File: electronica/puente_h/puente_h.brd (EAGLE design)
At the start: 100 x 80 mm, 40 parts, among them IC1 7805, IC2 7812, IC3 74HC04N, IC4 74HC08N, IC5 ADUM1400, Q1 IRF2804, Q2 IRF2804, Q5 IRF2804, Q6 IRF2804, U3 IR2110

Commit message: pads mas largos
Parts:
- removed JP2: (no value), pinhead:1X06
- removed U3: IR2110, components:IR2110
- added JP1: (no value), pinhead:1X06
- added U1: IR2110LP, components:IR2110-LP
- U$1: value IR2110 -> IR2110LP; device components:IR2110 -> components:IR2110-LP
- moved R18 137.3 mm to (66.3, 37.0), turned to 90 degrees
- moved C8 134.8 mm to (67.3, 106.7)
- moved Q5 121.9 mm to (57.1, 38.5), turned to 90 degrees
- moved MOTOR 121.4 mm to (38.2, 11.0), turned to 180 degrees
- moved R20 121.3 mm to (70.9, 20.6), turned to 270 degrees
- moved IC5 118.4 mm to (24.4, 106.2), turned to 180 degrees
- moved C3 118.1 mm to (53.1, 110.7), turned to 180 degrees
- moved R17 118.0 mm to (65.3, 52.5), turned to 180 degrees
- moved D9 105.1 mm to (66.5, 21.0), turned to 270 degrees
- moved D7 105.1 mm to (33.1, 57.7), turned to 180 degrees
- moved IC3 104.6 mm to (13.0, 86.2)
- moved IC2 102.4 mm to (50.3, 102.4), turned to 180 degrees
- moved R19 100.2 mm to (70.6, 36.7), turned to 270 degrees
- moved C1 99.1 mm to (49.1, 93.7)
- moved IN 92.0 mm to (61.0, 118.1), turned to 180 degrees
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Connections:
- removed net GND1@2: C7.2, IC5.2, IC5.8, JP2.2
- removed net N$13: IC5.4, JP2.4
- removed net N$14: IC5.5, JP2.5
- removed net N$8: IC5.3, JP2.3
- new net N$20: IC5.6, JP1.1
- new net N$21: IC5.4, JP1.3
- new net N$22: IC5.3, JP1.4
- new net N$24: C7.1, IC5.1, JP1.6
- net +12V: now also U1.3; no longer U3.3
- net +5V: now also U1.9; no longer U3.9
- net GND: now also U1.13, U1.2; no longer U3.13, U3.2
- net N$1: now also U1.6; no longer U$1.6
- net N$11: now also U1.10; no longer U$1.10
- net N$12: now also U1.12; no longer U$1.12
- net N$15: now also IC5.5, JP1.2; no longer IC5.6, JP2.6
- net N$19: now also U$1.12; no longer U3.12
- net N$2: now also U1.7; no longer U$1.7
- net N$3: now also U1.5; no longer U$1.5
- net N$30: now also U$1.6; no longer U3.6
- net N$31: now also U$1.5; no longer U3.5
- net N$32: now also U$1.7; no longer U3.7
- net N$35: now also U$1.1; no longer U3.1
- net N$5: now also C7.2, IC5.2, IC5.8, JP1.5; no longer C7.1, IC5.1, JP2.1
- net N$6: now also U1.1; no longer U$1.1
- net N$9: now also U$1.10; no longer U3.10
- net SD: now also U1.11; no longer U3.11
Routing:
- net GND: track 0.00 -> 246.0 mm
- net +5V: track 0.00 -> 112.4 mm
- net +12V: track 0.00 -> 80.4 mm
- net N$35: track 0.00 -> 76.8 mm
- net N$3: track 0.00 -> 70.1 mm
- net N$31: track 0.00 -> 65.8 mm
- net N$6: track 0.00 -> 49.8 mm
- net A: track 0.00 -> 42.7 mm, vias 0 -> 1
- net B: track 0.00 -> 41.2 mm
- net N$30: track 0.00 -> 40.7 mm
- net EN: track 0.00 -> 38.3 mm
- net N$4: track 0.00 -> 31.2 mm
- net N$12: track 0.00 -> 30.8 mm
- net N$7: track 0.00 -> 30.1 mm
- net N$5: track 0.00 -> 27.8 mm
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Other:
- board size 100 x 80 mm -> 80.2 x 123.2 mm

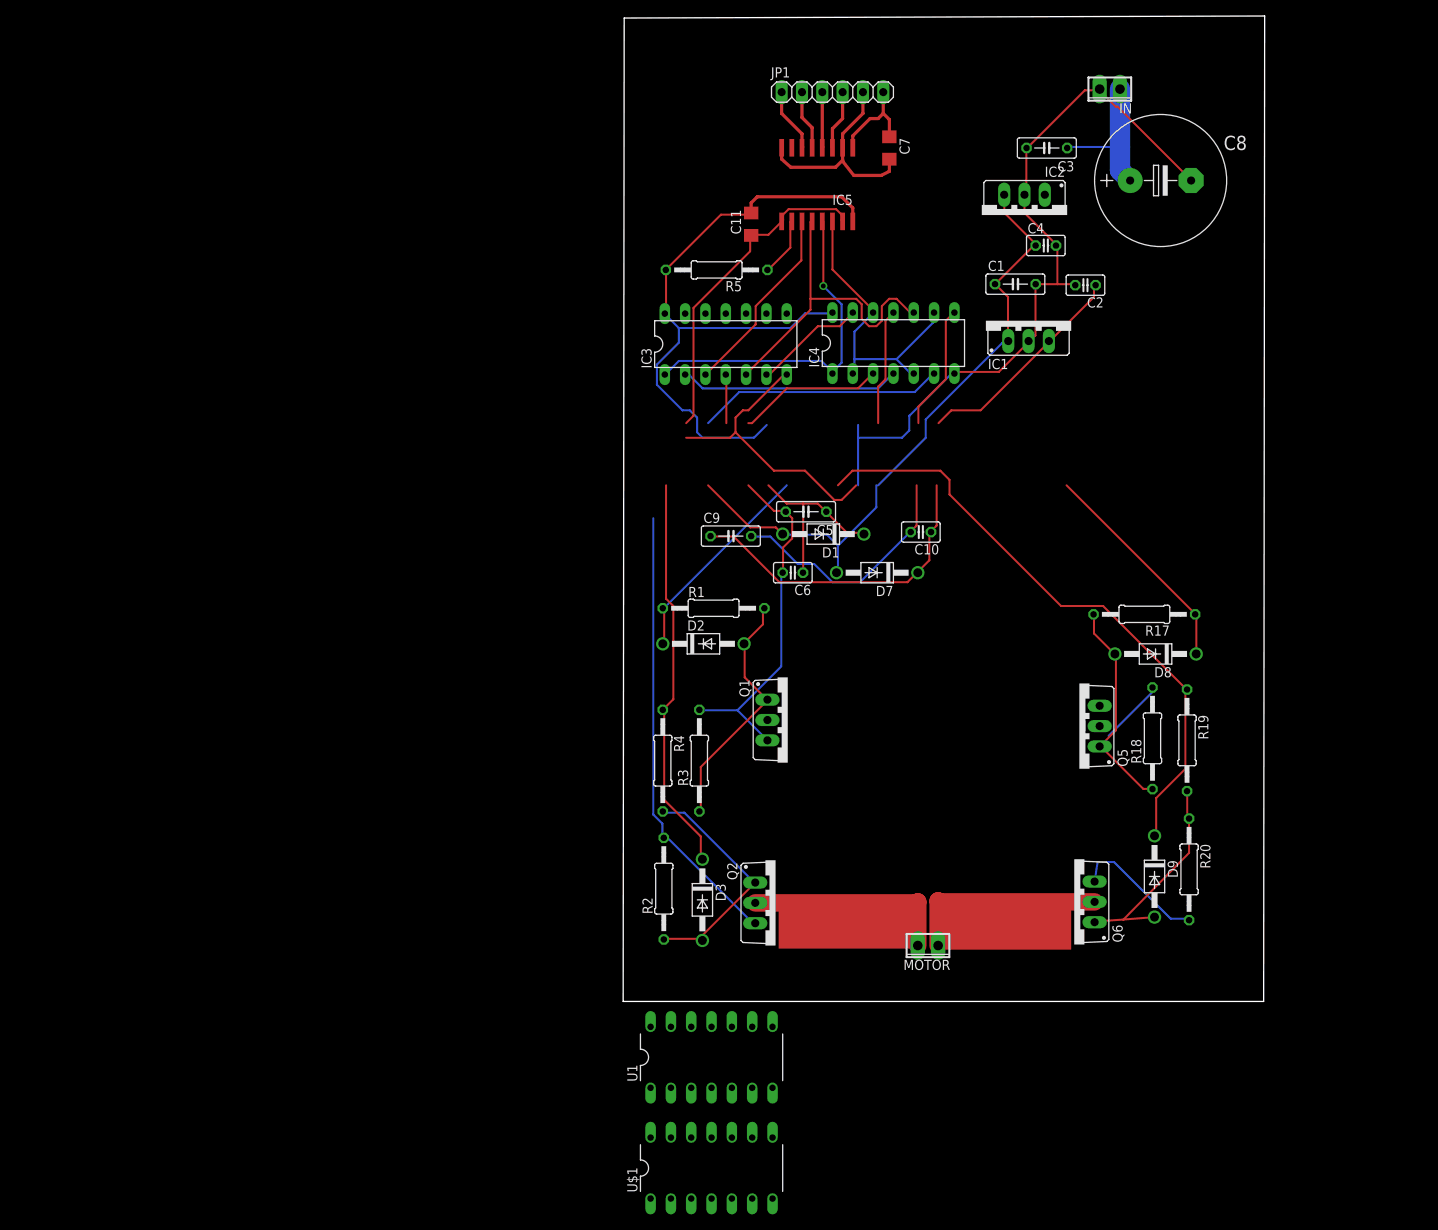
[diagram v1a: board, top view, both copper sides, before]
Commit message: packages con pad mas largos, nuevo pcb
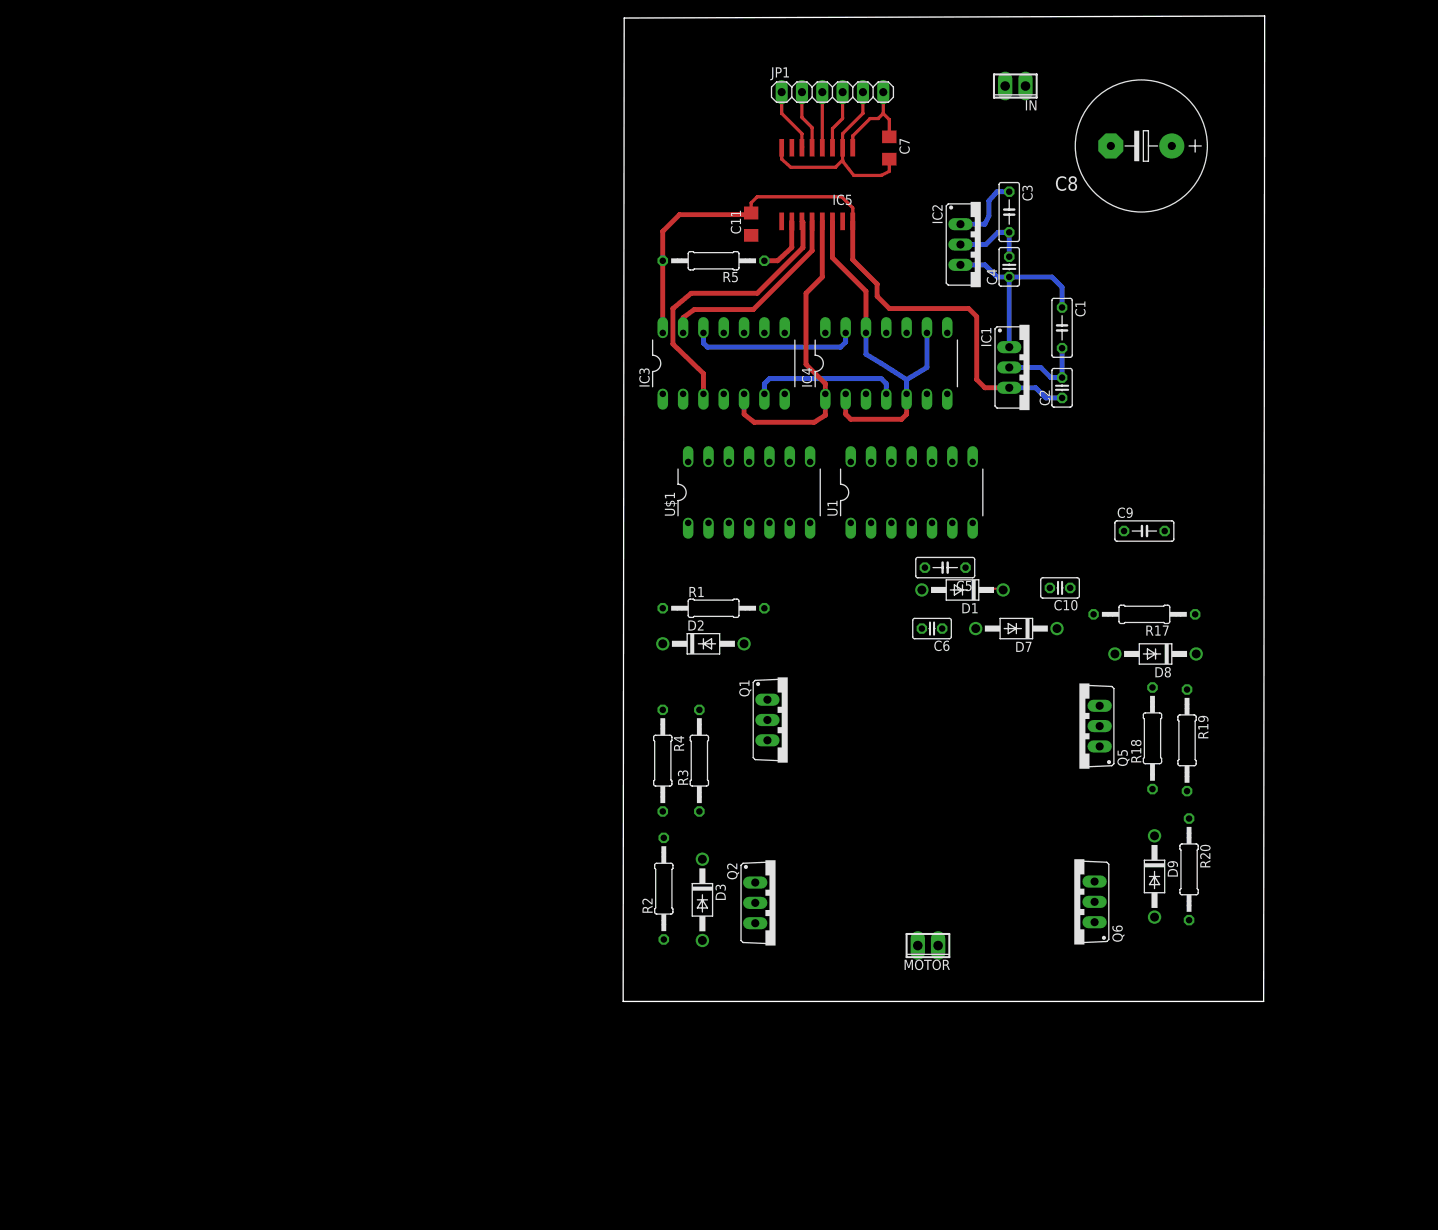
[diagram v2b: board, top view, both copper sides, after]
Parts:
- IC3: value 74HC04N -> 7404LP; device 74xx-eu:DIL14 -> components:IR2110-LP
- IC4: value 74HC08N -> 7408LP; device 74xx-eu:DIL14 -> components:IR2110-LP
- moved U$1 84.6 mm to (14.6, 67.7)
- moved U1 74.9 mm to (34.9, 67.7)
- moved C9 51.7 mm to (65.3, 62.9)
- moved C5 18.7 mm to (40.4, 58.3)
- moved C10 18.7 mm to (54.7, 55.8)
- moved C6 18.7 mm to (38.7, 50.7)
- moved D1 18.7 mm to (43.8, 55.5)
- moved D7 18.7 mm to (50.5, 50.7)
- moved C2 13.2 mm to (55.0, 80.8), turned to 90 degrees
- moved IN 11.8 mm to (49.1, 118.5)
- moved C3 9.28 mm to (48.4, 102.7), turned to 270 degrees
- moved C1 8.00 mm to (55.0, 88.3), turned to 270 degrees
- moved IC2 6.59 mm to (44.8, 98.7), turned to 270 degrees
- moved IC1 5.84 mm to (50.9, 83.3), turned to 270 degrees
- moved C4 5.29 mm to (48.4, 95.9), turned to 90 degrees
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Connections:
- net A: now also IC3.5; no longer IC3.1
- net B: now also IC3.13; no longer IC3.5
- net N$10: now also IC3.6; no longer IC3.2
- net N$17: now also IC3.12; no longer IC3.6
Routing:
- net GND: track 246.0 -> 20.6 mm
- net N$35: track 76.8 -> 0.00 mm
- net N$3: track 70.1 -> 0.00 mm
- net N$31: track 65.8 -> 0.00 mm
- net +12V: track 80.4 -> 25.2 mm
- net N$6: track 49.8 -> 0.00 mm
- net N$30: track 40.7 -> 0.19 mm
- net N$4: track 31.2 -> 0.00 mm
- net N$12: track 30.8 -> 0.00 mm
- net N$7: track 30.1 -> 1.46 mm
- net N$32: track 27.8 -> 0.15 mm
- net +5V: track 112.4 -> 84.9 mm
- net N$33: track 27.3 -> 0.00 mm
- net N$36: track 27.1 -> 0.55 mm
- net N$2: track 26.4 -> 0.49 mm
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
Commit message: mejores posiciones
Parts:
- moved D1 32.6 mm to (11.3, 58.0)
- moved C6 32.0 mm to (6.86, 53.1)
- moved D8 29.2 mm to (38.9, 45.3)
- moved R17 26.6 mm to (38.9, 49.8)
- moved C5 26.0 mm to (14.9, 53.2)
- moved C9 25.7 mm to (41.1, 54.1), turned to 180 degrees
- moved U1 23.5 mm to (11.4, 67.9)
- moved C10 20.8 mm to (34.0, 54.1)
- moved U$1 17.4 mm to (32.0, 67.9)
- moved D7 14.5 mm to (38.5, 58.8)
- moved R19 13.0 mm to (57.7, 38.2)
- moved R20 12.7 mm to (58.2, 19.6), turned to 90 degrees
- moved R18 12.5 mm to (53.8, 38.4)
- moved D9 12.1 mm to (54.5, 19.8)
- moved Q5 11.6 mm to (45.6, 37.7)
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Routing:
- net GND: track 20.6 -> 67.6 mm
- net SD: track 0.00 -> 31.4 mm
- net N$11: track 0.00 -> 24.8 mm
- net +12V: track 25.2 -> 48.1 mm
- net +5V: track 84.9 -> 98.6 mm
- net N$1: track 2.37 -> 0.00 mm
- net N$7: track 1.46 -> 0.23 mm
- net N$36: track 0.55 -> 0.00 mm
- net N$10: track 18.3 -> 18.8 mm

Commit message: ruteo mejorado
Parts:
- moved IN 53.7 mm to (65.9, 67.4), turned to 90 degrees
- moved C8 44.1 mm to (54.4, 68.2), turned to 90 degrees
- moved C10 25.7 mm to (59.7, 55.9)
- moved D8 18.3 mm to (57.1, 45.7)
- moved R17 15.8 mm to (54.6, 50.8)
- moved D1 13.0 mm to (22.9, 52.1), turned to 270 degrees
- moved C9 9.81 mm to (50.8, 55.9), turned to 0 degrees
- moved D7 9.00 mm to (44.5, 52.1), turned to 270 degrees
- moved MOTOR 4.64 mm to (29.1, 9.14)
- moved D2 4.37 mm to (12.7, 47.0)
- moved R19 4.24 mm to (61.0, 35.6)
- moved Q5 4.05 mm to (42.2, 35.6), turned to 270 degrees
- moved C11 3.39 mm to (15.4, 104.5)
- moved Q6 3.30 mm to (42.2, 17.8), turned to 270 degrees
- moved Q1 3.24 mm to (20.3, 35.6)
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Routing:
- net GND: track 67.6 -> 216.1 mm
- net N$31: track 0.00 -> 136.8 mm
- net VIN: track 9.14 -> 141.6 mm
- net N$3: track 0.00 -> 119.9 mm
- net N$35: track 0.00 -> 83.2 mm
- net +12V: track 48.1 -> 120.8 mm
- net N$6: track 0.00 -> 58.1 mm
- net N$32: track 0.00 -> 44.7 mm, vias 0 -> 1
- net N$2: track 0.00 -> 40.8 mm
- net N$30: track 0.00 -> 30.0 mm
- net N$36: track 0.00 -> 27.3 mm
- net N$33: track 0.00 -> 26.9 mm
- net N$1: track 0.00 -> 26.1 mm
- net N$4: track 0.00 -> 22.9 mm
- net N$19: track 0.00 -> 22.8 mm
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
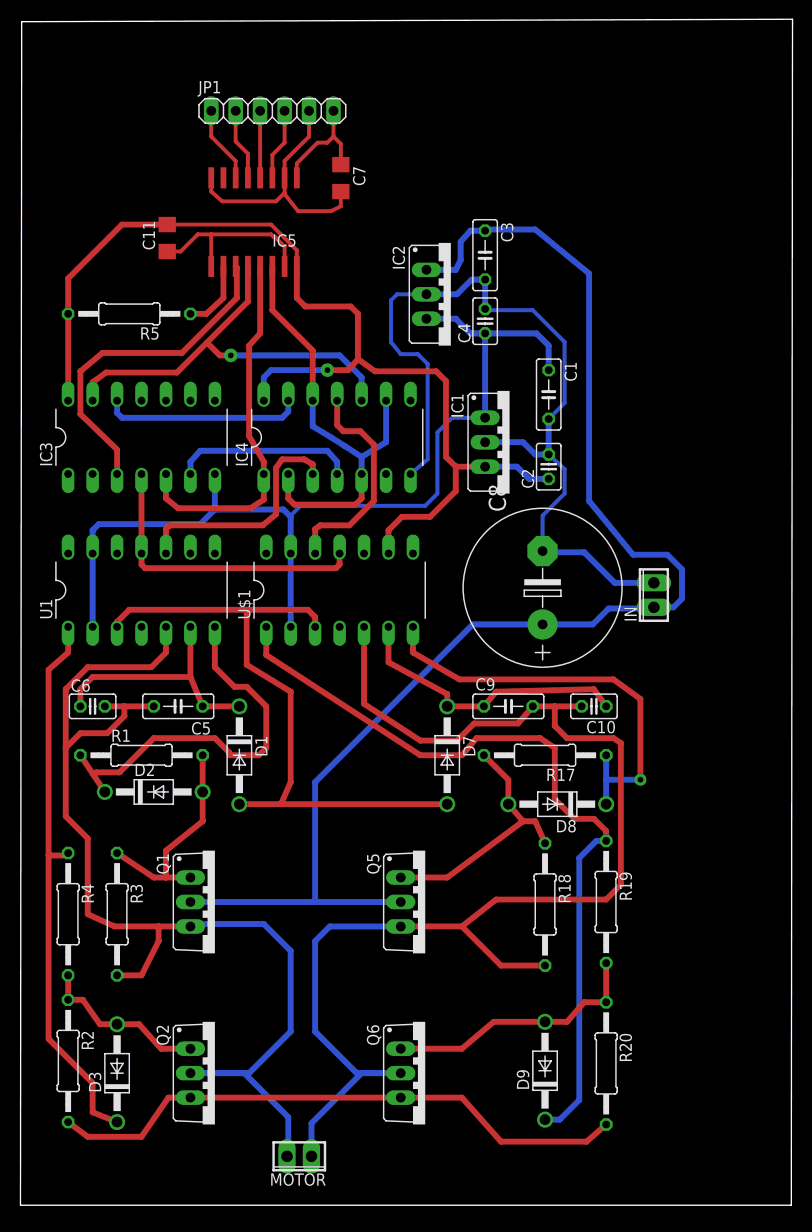
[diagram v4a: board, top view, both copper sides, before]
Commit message: ruteo con poligonos
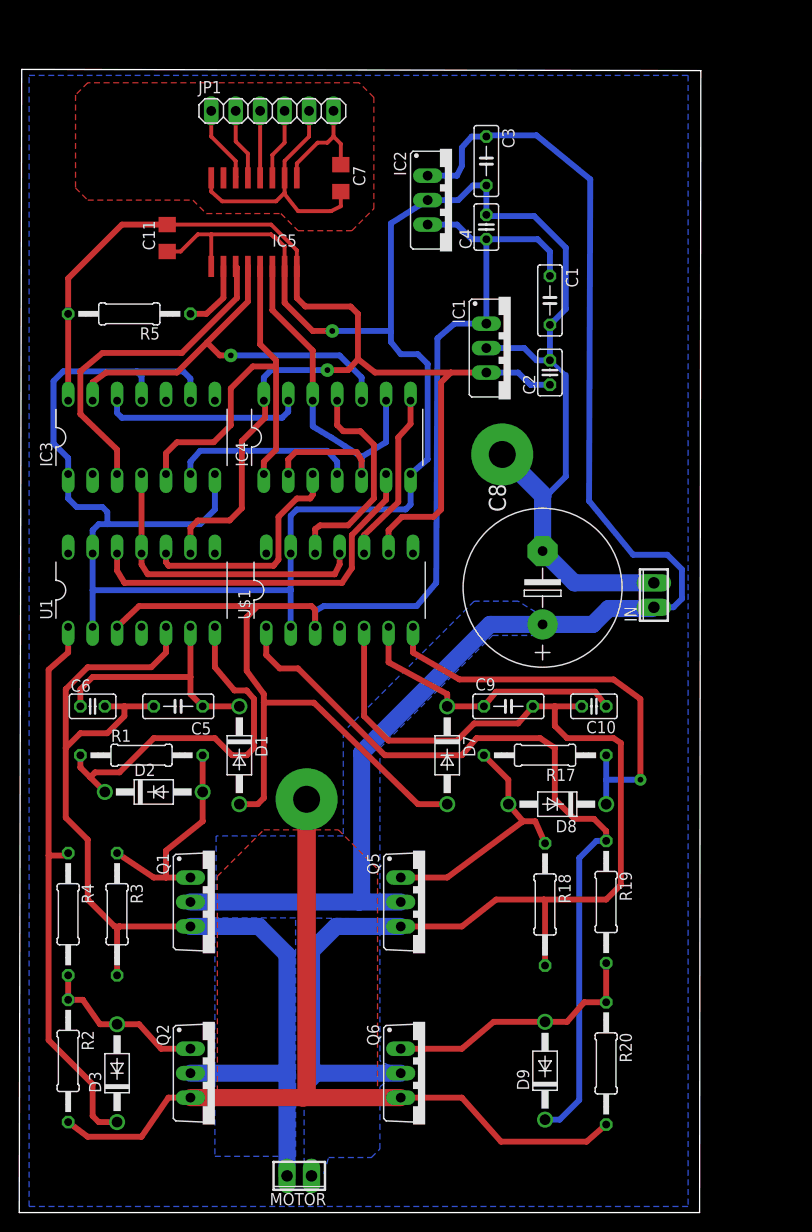
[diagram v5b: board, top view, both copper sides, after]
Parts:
- moved C3 9.78 mm to (48.5, 112.5)
- moved C1 9.78 mm to (55.1, 98.0)
- moved C2 9.78 mm to (55.1, 90.6)
- moved C4 9.78 mm to (48.5, 105.7)
- moved IC1 9.78 mm to (51.1, 93.1)
- moved IC2 9.78 mm to (45.0, 108.5)
- moved MOTOR 2.03 mm to (29.1, 7.11)
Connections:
- net N$3 renamed POWER-M2
- net N$31 renamed POWER-M1
- net N$5 renamed GND-IN
- net GND: now also IC3.1, IC3.11, IC3.9
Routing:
- net GND: track 216.1 -> 355.8 mm, vias 0 -> 3
- net N$12: track 0.00 -> 38.9 mm
- net +5V: track 112.8 -> 135.1 mm
- net +12V: track 120.8 -> 142.2 mm
- net N$9: track 0.00 -> 17.9 mm
- net POWER-M1: track 136.8 -> 123.2 mm
- net POWER-M2: track 119.9 -> 112.3 mm
- net VIN: track 141.6 -> 148.3 mm
- net A: track 38.4 -> 42.3 mm
- net EN: track 46.6 -> 44.8 mm
- net N$2: track 40.8 -> 39.5 mm
- net N$35: track 83.2 -> 84.5 mm
- net SD: track 31.4 -> 32.3 mm
- net N$11: track 24.8 -> 24.2 mm
- added copper zone on layer 1, net GND
- added copper zone on layer 1, net GND-IN
- added copper zone on layer 16, net N$5
- added copper zone on layer 16, net POWER-M1
- added copper zone on layer 16, net POWER-M2
- added copper zone on layer 16, net VIN
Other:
- board size 80.2 x 123.2 mm -> 70.8 x 118.7 mm

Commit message: puente h ok
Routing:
- added copper zone on layer 16, net GND
- removed copper zone on layer 16, net N$5
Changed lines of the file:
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@@
 <wire x1="55.118" y1="78.105" x2="54.61" y2="78.105" width="0.6096" layer="16"/>
 <wire x1="54.61" y1="78.105" x2="54.356" y2="77.851" width="0.6096" layer="16"/>
-<polygon width="0.4064" layer="1">
+<polygon width="0.4064" layer="1" isolate="0.6096" rank="2">
 <vertex x="30.734" y="43.053"/>
 <vertex x="33.02" y="43.053"/>
@@
 <wire x1="17.78" y1="89.916" x2="17.018" y2="90.678" width="0.6096" layer="16"/>
 <wire x1="17.018" y1="90.678" x2="12.192" y2="90.678" width="0.6096" layer="16"/>
-<wire x1="29.845" y1="46.228" x2="28.194" y2="64.135" width="0" layer="19" extent="1-1"/>
+<polygon width="0.6096" layer="16" isolate="0.6096" rank="6">
+<vertex x="1.016" y="121.412"/>
+<vertex x="69.469" y="121.412"/>
+<vertex x="69.469" y="3.937"/>
+<vertex x="1.016" y="3.937"/>
+</polygon>
 </signal>
 <signal name="VIN">
@@
 <wire x1="35.56" y1="51.054" x2="35.56" y2="35.814" width="1.778" layer="16"/>
 <wire x1="35.56" y1="35.814" x2="35.306" y2="35.56" width="1.778" layer="16"/>
-<polygon width="0.4064" layer="16" thermals="no">
+<polygon width="0.4064" layer="16" isolate="0.6096" thermals="no" rank="2">
 <vertex x="20.447" y="34.798"/>
 <vertex x="37.592" y="34.798"/>
@@
 <wire x1="24.892" y1="33.02" x2="17.78" y2="33.02" width="1.778" layer="16"/>
 <wire x1="17.78" y1="17.78" x2="27.813" y2="17.78" width="1.778" layer="16"/>
-<polygon width="0.4064" layer="16">
+<polygon width="0.4064" layer="16" isolate="0.6096" rank="2">
 <vertex x="20.32" y="33.909"/>
 <vertex x="20.32" y="9.144"/>
@@
 <wire x1="39.624" y1="17.78" x2="30.861" y2="17.78" width="1.778" layer="16"/>
 <wire x1="30.861" y1="17.78" x2="30.353" y2="17.272" width="0.6096" layer="16"/>
-<polygon width="0.4064" layer="16" thermals="no">
+<polygon width="0.4064" layer="16" isolate="0.6096" thermals="no" rank="2">
 <vertex x="29.591" y="33.909"/>
 <vertex x="29.591" y="7.366"/>
@@
 <signal name="N$27">
 </signal>
-<signal name="N$5">
-<polygon width="0.6096" layer="16">
-<vertex x="1.016" y="121.412"/>
-<vertex x="69.469" y="121.412"/>
-<vertex x="69.469" y="3.937"/>
-<vertex x="1.016" y="3.937"/>
-</polygon>
-</signal>
 </signals>

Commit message: placas nuevas
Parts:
- removed IN, MOTOR: (no value), con-phoenix-254:2POL254
- added CON-IN, CON-MOTOR: METALTEX-2, components:METALTEX-2
- moved C8 6.90 mm to (55.1, 61.3)
- moved R19 5.54 mm to (64.3, 31.1)
- moved C10 5.54 mm to (63.0, 51.4)
- moved C9 5.54 mm to (54.1, 51.4)
- moved D7 5.54 mm to (47.8, 47.6)
- moved D8 5.54 mm to (60.5, 41.3)
- moved R17 5.54 mm to (57.9, 46.4)
- moved D9 5.54 mm to (57.9, 12.3)
- moved R20 5.54 mm to (64.3, 14.4)
- moved R18 5.54 mm to (57.9, 30.9)
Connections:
- net GND: now also CON-IN.P2; no longer IN.2
- net POWER-M1: now also CON-MOTOR.P2; no longer MOTOR.1
- net POWER-M2: now also CON-MOTOR.P1; no longer MOTOR.2
- net VIN: now also CON-IN.P1; no longer IN.1
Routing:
- net GND: track 355.8 -> 316.8 mm
- net POWER-M2: track 112.3 -> 101.6 mm
- net +12V: track 142.2 -> 151.8 mm
- net N$32: track 44.7 -> 50.9 mm
- net VIN: track 148.3 -> 143.0 mm
- net N$35: track 84.5 -> 89.3 mm
- net N$30: track 29.9 -> 34.7 mm
- net N$33: track 26.9 -> 31.4 mm
- net POWER-M1: track 123.2 -> 126.3 mm
- net N$36: track 27.3 -> 30.3 mm
